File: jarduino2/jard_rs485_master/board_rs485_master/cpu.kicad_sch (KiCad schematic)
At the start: 4 parts, among them U1 RtcArduino

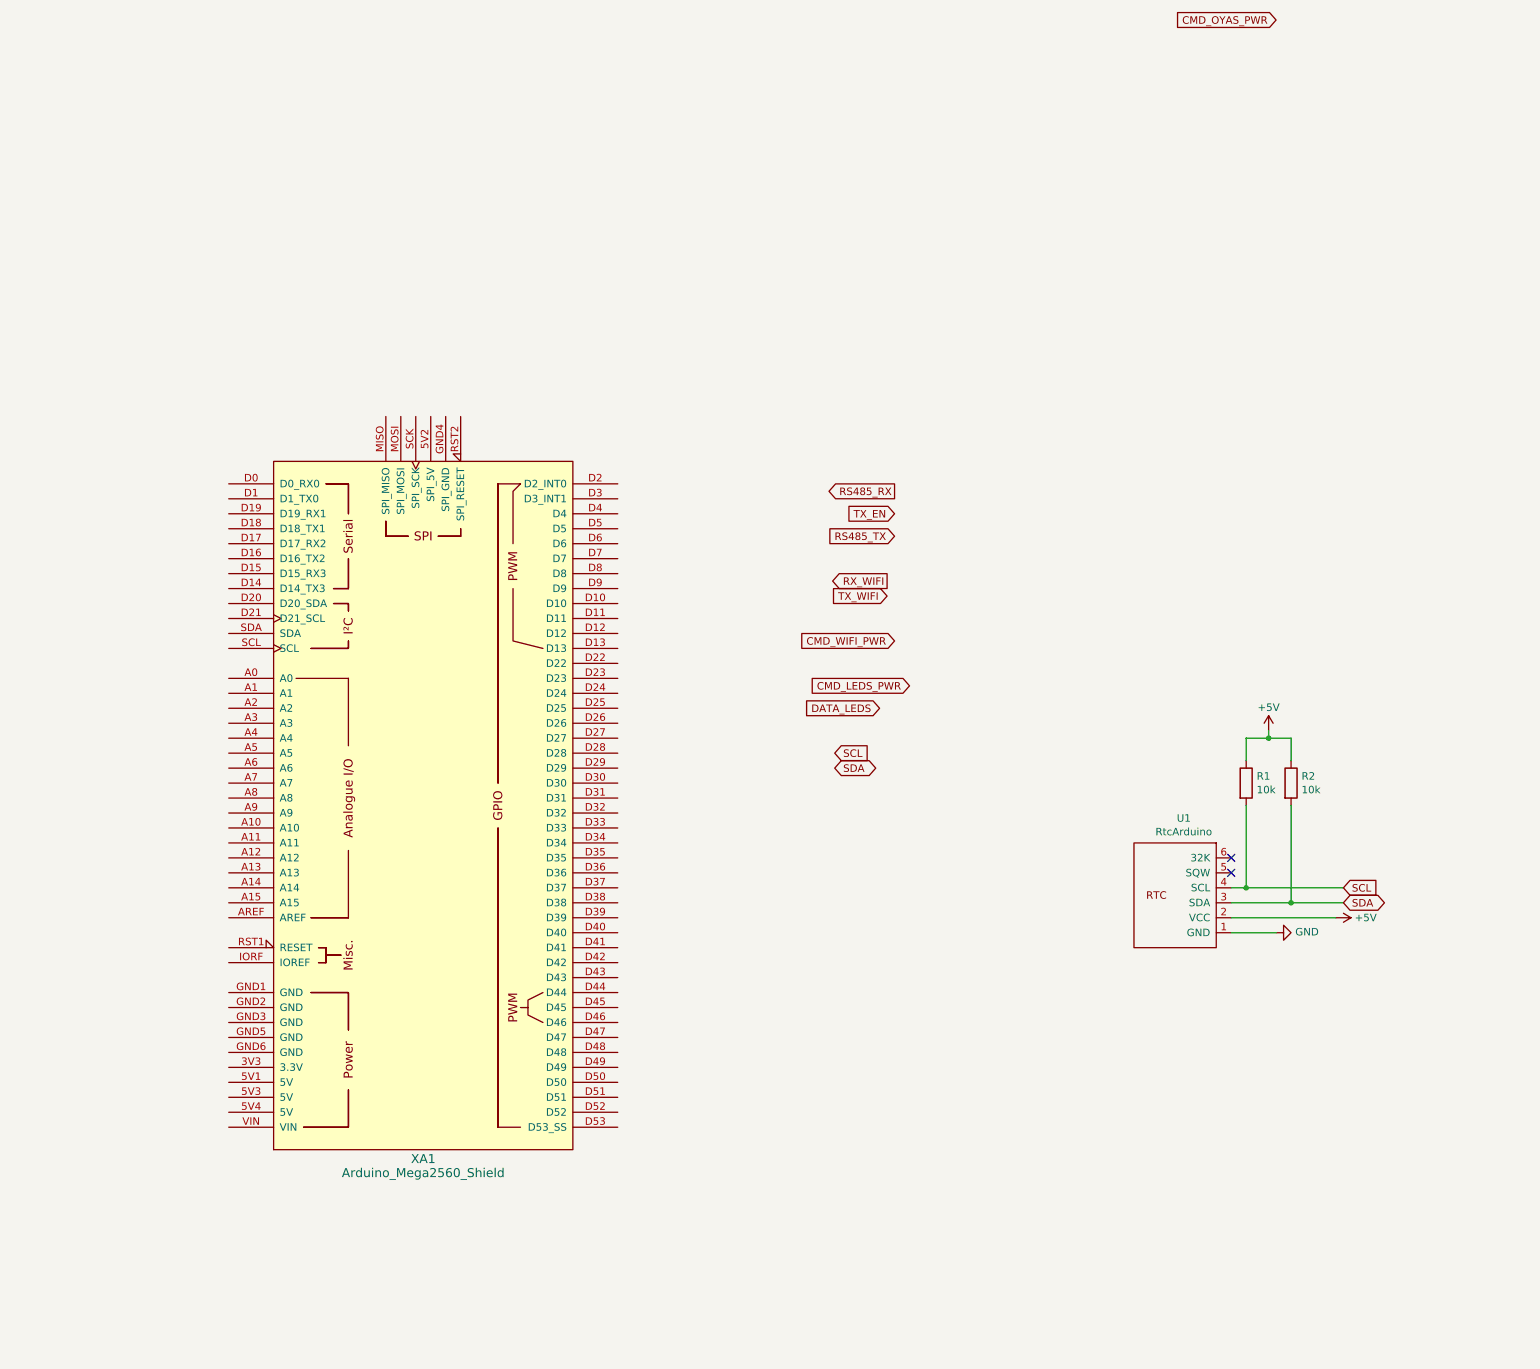
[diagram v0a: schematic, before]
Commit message: Candidate pour revue du master Oyas (avec modules en tant que shield MEGA)
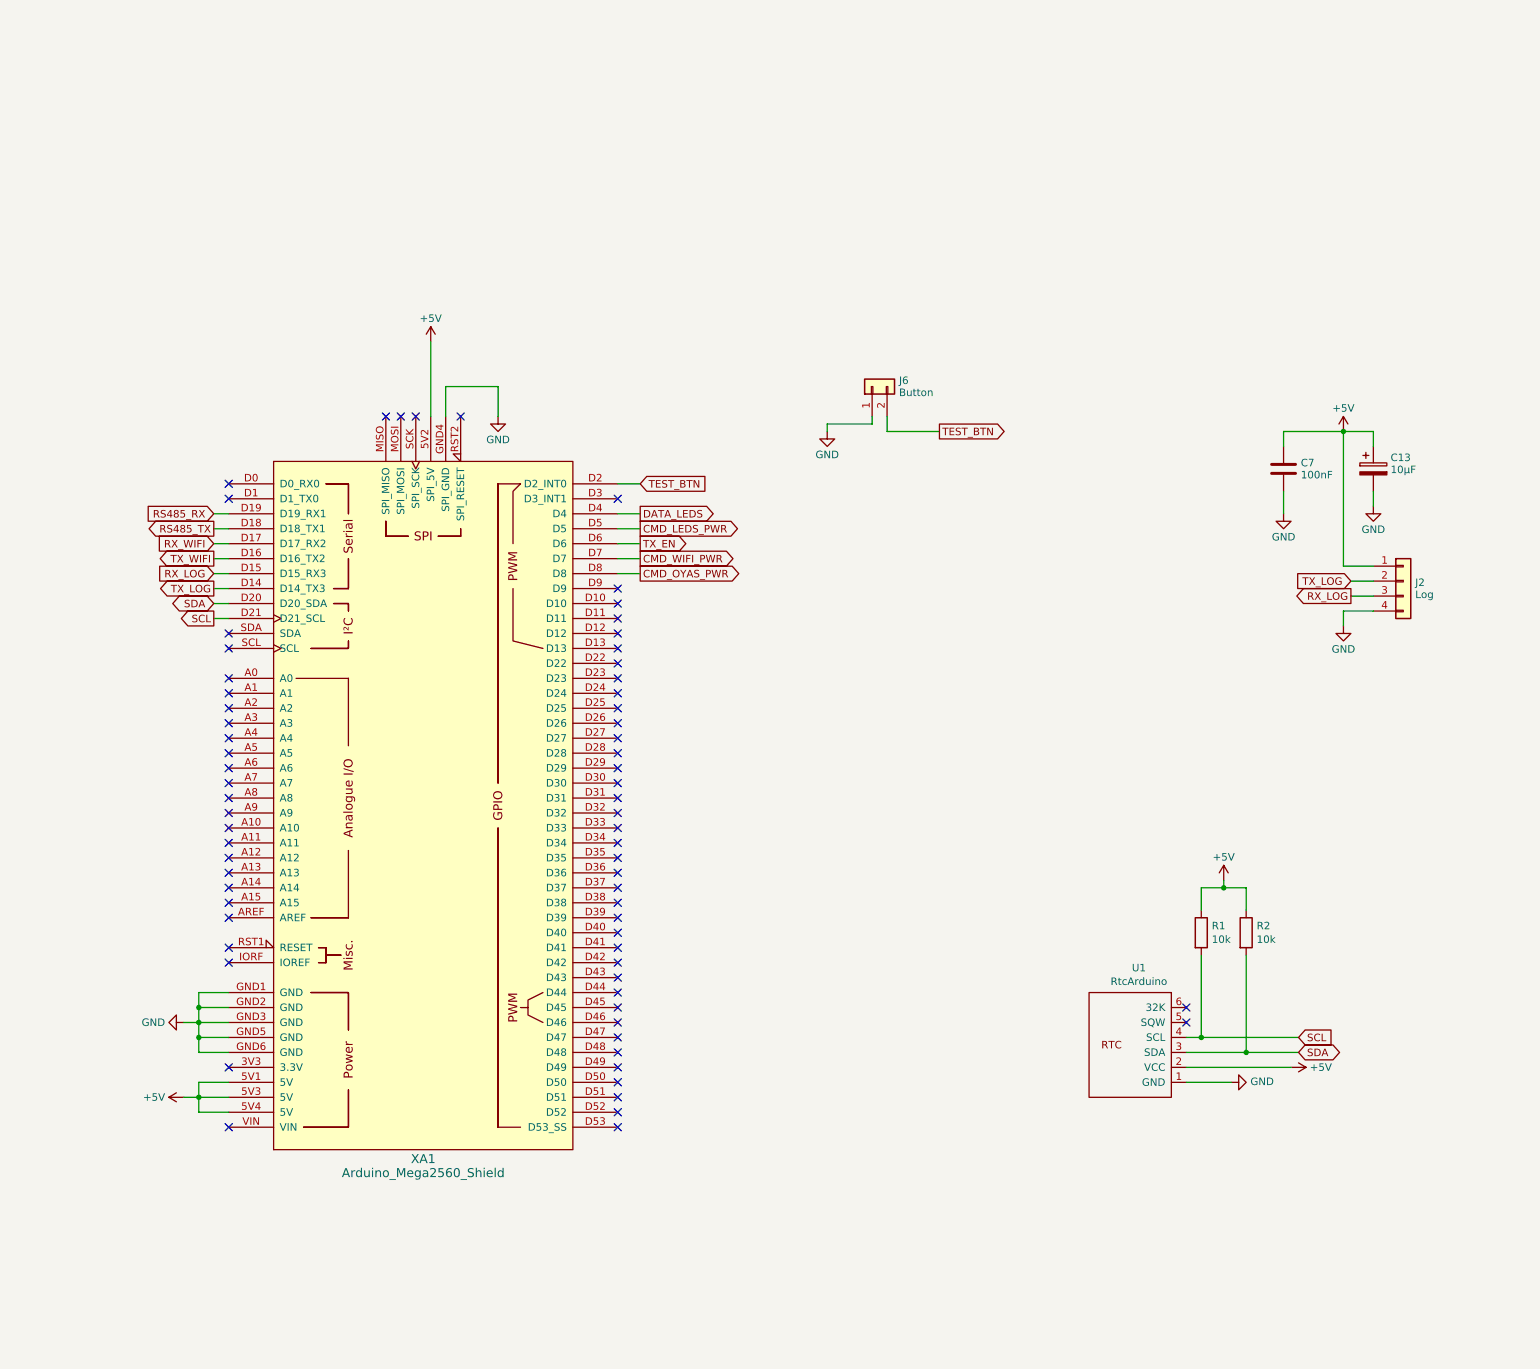
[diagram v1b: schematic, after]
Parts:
- added C13: 10µF, Capacitor_THT:CP_Radial_D4.0mm_P2.00mm, symbol Device:C_Polarized
- added C7: 100nF, Capacitor_THT:C_Disc_D5.0mm_W2.5mm_P2.50mm, symbol Device:C
- added J2: Log, Connector_JST:JST_XH_B4B-XH-AM_1x04_P2.50mm_Vertical, symbol Connector_Generic:Conn_01x04
- added J6: Button, Connector_PinHeader_2.54mm:PinHeader_1x02_P2.54mm_Vertical, symbol Connector_Generic:Conn_01x02
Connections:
- net +5V: now also XA1.5V1 (5V), XA1.5V2 (SPI_5V), XA1.5V3 (5V), XA1.5V4 (5V), C13.1, C7.1, J2.1 (Pin_1)
- net CMD_LEDS_PWR: now also XA1.D5
- net CMD_OYAS_PWR: now also XA1.D8
- net CMD_WIFI_PWR: now also XA1.D7
- net DATA_LEDS: now also XA1.D4
- net GND: now also XA1.GND1 (GND), XA1.GND2 (GND), XA1.GND3 (GND), XA1.GND4 (SPI_GND), XA1.GND5 (GND), XA1.GND6 (GND), C13.2, C7.2, J2.4 (Pin_4), J6.1 (Pin_1)
- net RS485_RX: now also XA1.D19 (D19_RX1)
- net RS485_TX: now also XA1.D18 (D18_TX1)
- net RX_WIFI: now also XA1.D17 (D17_RX2)
- net SCL: now also XA1.D21 (D21_SCL)
- net SDA: now also XA1.D20 (D20_SDA)
- net TX_EN: now also XA1.D6
- net TX_WIFI: now also XA1.D16 (D16_TX2)
- net TX_LOG: now reaches XA1.D14 (D14_TX3)
- net TX_LOG: now also J2.2 (Pin_2)
- net RX_LOG: now reaches XA1.D15 (D15_RX3)
- net RX_LOG: now also J2.3 (Pin_3)
- net TEST_BTN: now reaches XA1.D2 (D2_INT0)
- net TEST_BTN: now also J6.2 (Pin_2)
- no-connect marks 2 -> 69
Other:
- company: (none) -> BPC
- title: (none) -> Commande des OYA - Maître RS485
- moved on the sheet: R1, R2, U1

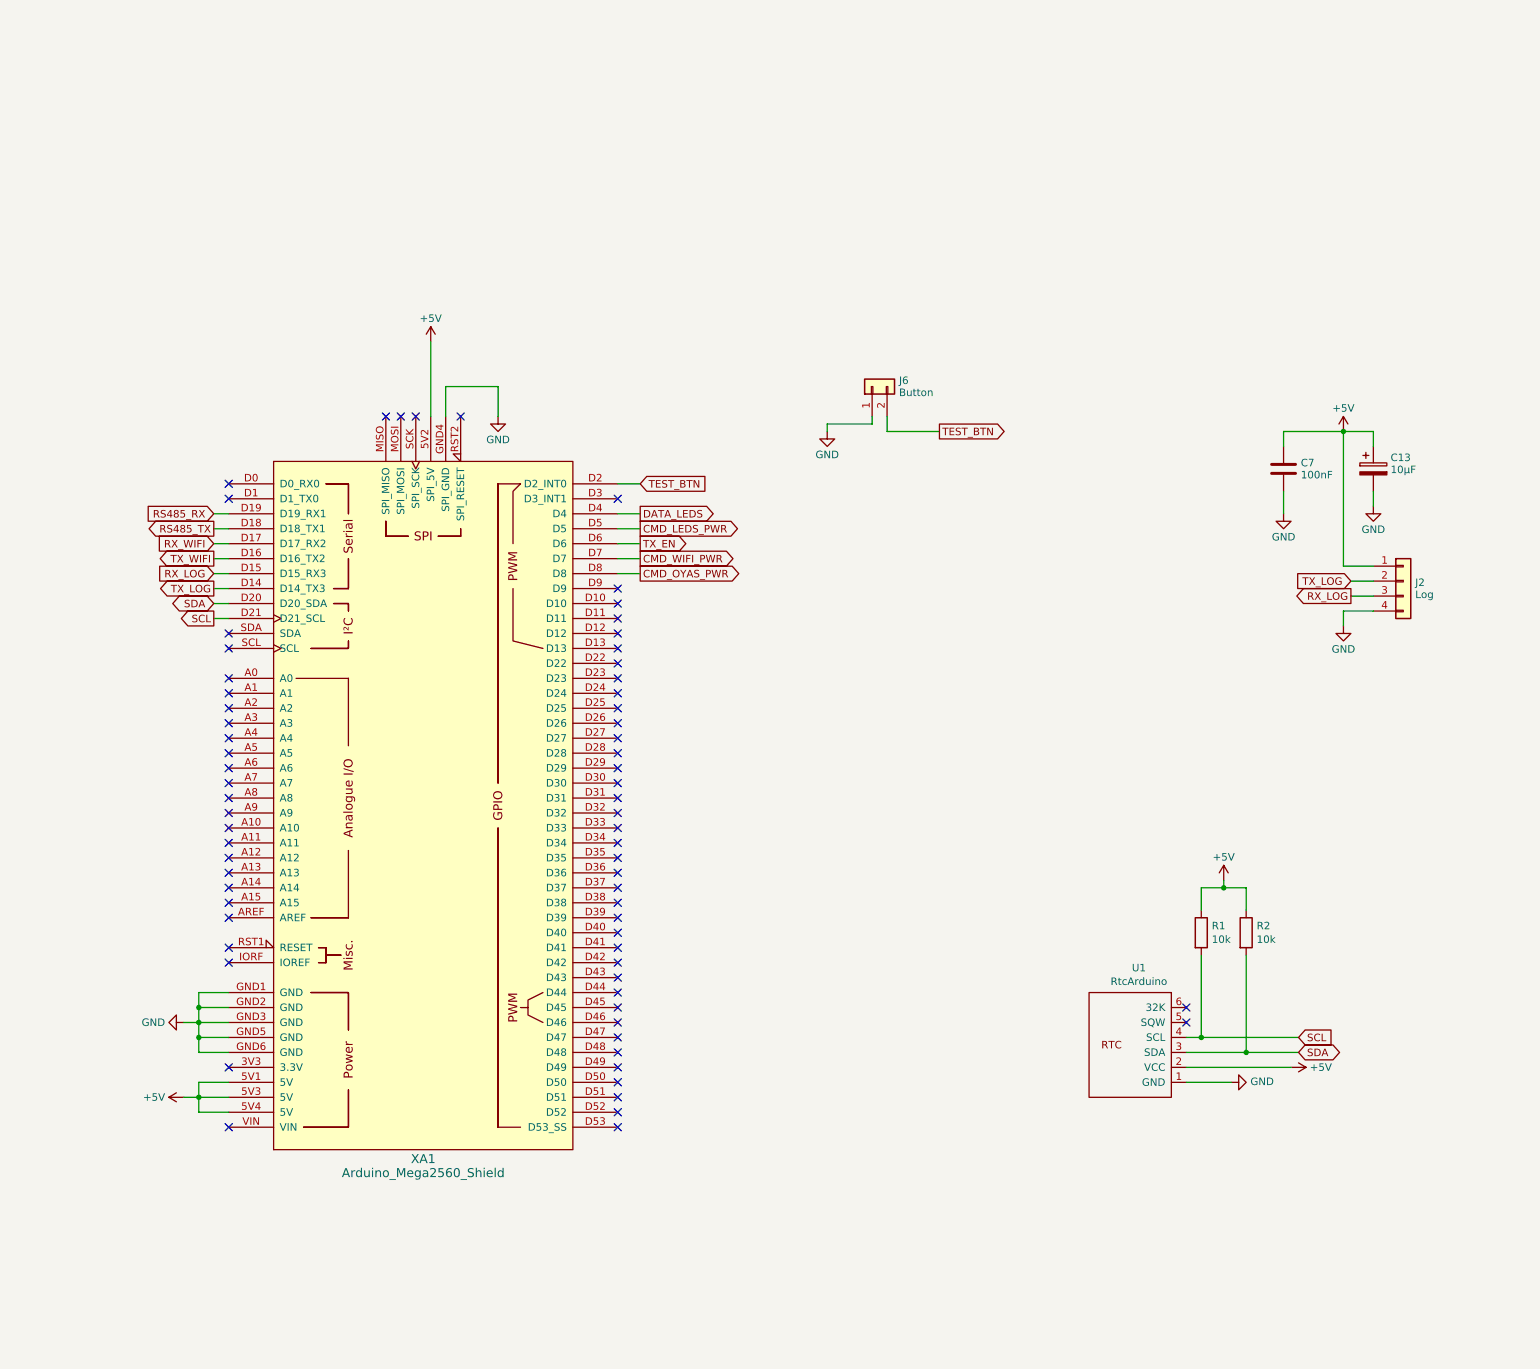
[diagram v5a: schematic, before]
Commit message: Titres + finitions (vias)
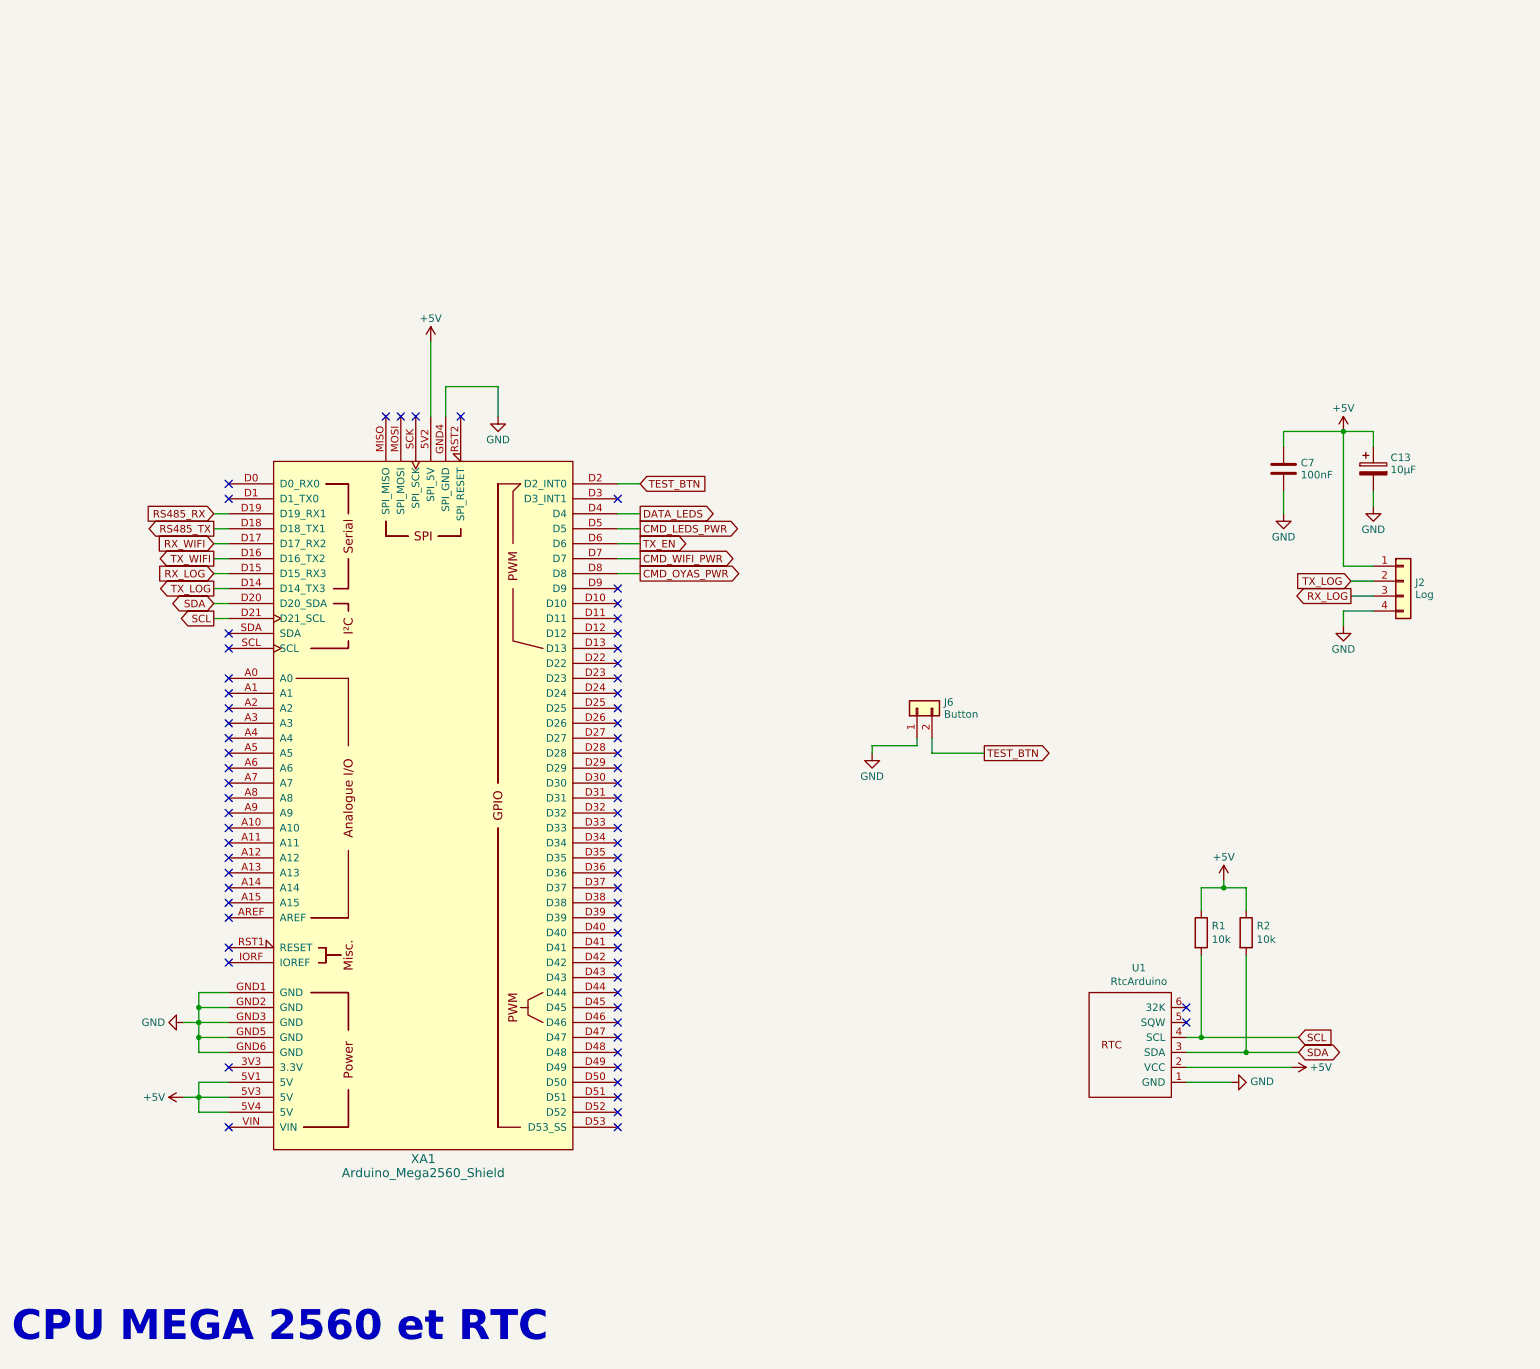
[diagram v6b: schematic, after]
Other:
- note added: "CPU MEGA 2560 et RTC"
- moved on the sheet: J6
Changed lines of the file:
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@@
     (stroke (width 0) (type default))
   )
-  (wire (pts (xy 166.37 33.02) (xy 166.37 35.56))
+  (wire (pts (xy 173.99 87.63) (xy 173.99 90.17))
     (stroke (width 0) (type default))
   )
@@
     (stroke (width 0) (type default))
   )
-  (wire (pts (xy 156.21 35.56) (xy 156.21 34.29))
+  (wire (pts (xy 163.83 90.17) (xy 163.83 88.9))
     (stroke (width 0) (type default))
   )
@@
     (stroke (width 0) (type default))
   )
-  (wire (pts (xy 166.37 35.56) (xy 175.26 35.56))
-    (stroke (width 0) (type default))
-  )
-  (wire (pts (xy 163.83 33.02) (xy 163.83 34.29))
+  (wire (pts (xy 173.99 90.17) (xy 182.88 90.17))
+    (stroke (width 0) (type default))
+  )
+  (wire (pts (xy 171.45 87.63) (xy 171.45 88.9))
     (stroke (width 0) (type default))
   )
@@
     (stroke (width 0) (type default))
   )
-  (wire (pts (xy 156.21 34.29) (xy 163.83 34.29))
-    (stroke (width 0) (type default))
+  (wire (pts (xy 163.83 88.9) (xy 171.45 88.9))
+    (stroke (width 0) (type default))
+  )
+  (text "CPU MEGA 2560 et RTC" (at 17.78 190.5 0)
+    (effects (font (size 5.08 5.08) (thickness 2.54) bold) (justify left bottom))
   )
   (global_label "TX_LOG" (shape input) (at 245.11 60.96 180) (fields_autoplaced)
@@
     )
   )
-  (global_label "TEST_BTN" (shape output) (at 175.26 35.56 0)
-    (effects (font (size 1.27 1.27)) (justify left))
-    (property "Intersheetrefs" "${INTERSHEET_REFS}" (at 175.26 35.56 0)
+  (global_label "TEST_BTN" (shape output) (at 182.88 90.17 0)
+    (effects (font (size 1.27 1.27)) (justify left))
+    (property "Intersheetrefs" "${INTERSHEET_REFS}" (at 182.88 90.17 0)
       (effects (font (size 1.27 1.27)) hide)
     )
@@
     )
   )
-  (symbol (lib_id "Connector_Generic:Conn_01x02") (at 163.83 27.94 90) (unit 1)
-    (in_bom yes) (on_board yes) (dnp no) (fields_autoplaced)
-    (property "Reference" "J6" (at 168.402 26.916 90)
+  (symbol (lib_id "Connector_Generic:Conn_01x02") (at 171.45 82.55 90) (unit 1)
+    (in_bom yes) (on_board yes) (dnp no) (fields_autoplaced)
+    (property "Reference" "J6" (at 176.022 81.526 90)
       (effects (font (size 1.27 1.27)) (justify right))
     )
-    (property "Value" "Button" (at 168.402 28.964 90)
+    (property "Value" "Button" (at 176.022 83.574 90)
       (effects (font (size 1.27 1.27)) (justify right))
     )
-    (property "Footprint" "Connector_PinHeader_2.54mm:PinHeader_1x02_P2.54mm_Vertical" (at 163.83 27.94 0)
-      (effects (font (size 1.27 1.27)) hide)
-    )
-    (property "Datasheet" "~" (at 163.83 27.94 0)
+    (property "Footprint" "Connector_PinHeader_2.54mm:PinHeader_1x02_P2.54mm_Vertical" (at 171.45 82.55 0)
+      (effects (font (size 1.27 1.27)) hide)
+    )
+    (property "Datasheet" "~" (at 171.45 82.55 0)
       (effects (font (size 1.27 1.27)) hide)
     )
@@
     )
   )
-  (symbol (lib_id "power:GND") (at 156.21 35.56 0) (unit 1)
-    (in_bom yes) (on_board yes) (dnp no) (fields_autoplaced)
-    (property "Reference" "#PWR036" (at 156.21 41.91 0)
-      (effects (font (size 1.27 1.27)) hide)
-    )
-    (property "Value" "GND" (at 156.21 39.505 0)
-      (effects (font (size 1.27 1.27)))
-    )
-    (property "Footprint" "" (at 156.21 35.56 0)
-      (effects (font (size 1.27 1.27)) hide)
-    )
-    (property "Datasheet" "" (at 156.21 35.56 0)
-      (effects (font (size 1.27 1.27)) hide)
-    )
+  (symbol (lib_id "power:GND") (at 163.83 90.17 0) (unit 1)
+    (in_bom yes) (on_board yes) (dnp no) (fields_autoplaced)
+    (property "Reference" "#PWR036" (at 163.83 96.52 0)
+      (effects (font (size 1.27 1.27)) hide)
+    )
+    (property "Value" "GND" (at 163.83 94.115 0)
+      (effects (font (size 1.27 1.27)))
+    )
+    (property "Footprint" "" (at 163.83 90.17 0)
+      (effects (font (size 1.27 1.27)) hide)
+    )
+    (property "Datasheet" "" (at 163.83 90.17 0)
+      (effects (font (size 1.27 1.27)) hide)
+    )
